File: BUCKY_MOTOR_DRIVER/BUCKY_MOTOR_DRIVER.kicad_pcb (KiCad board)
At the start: 2 copper layers, 26 x 22.6 mm, 8 parts, among them J1 P_INPUTS, J2 INPUTS, J3 OUT, U1 IFX9201SG

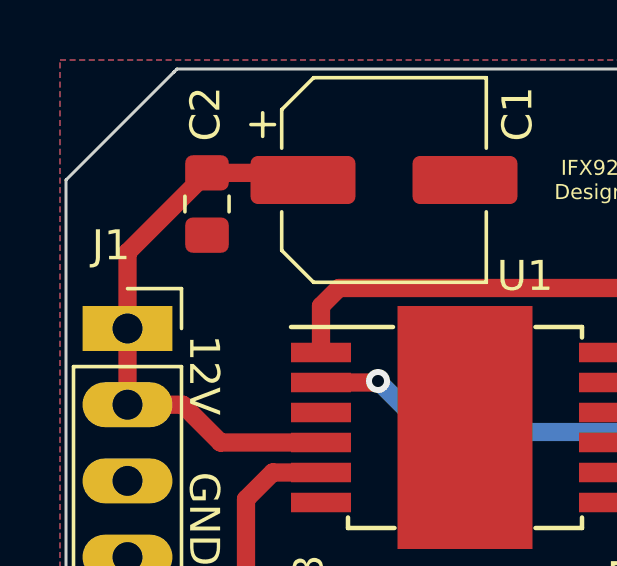
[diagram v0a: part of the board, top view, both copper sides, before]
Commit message: Finished up IR sch, Main, Started Power
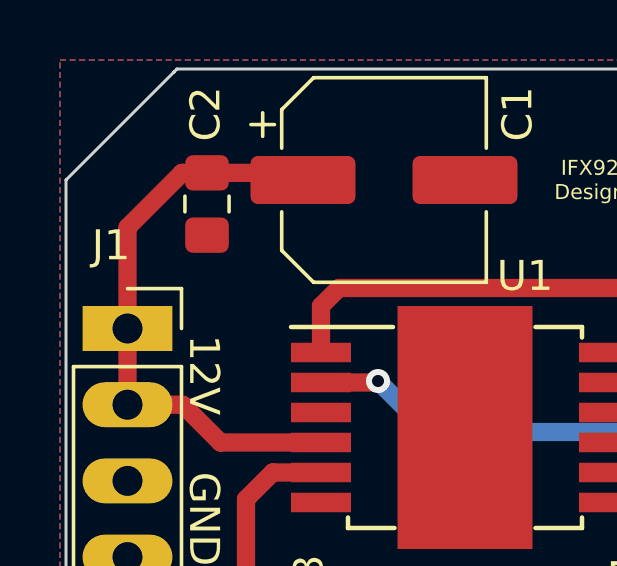
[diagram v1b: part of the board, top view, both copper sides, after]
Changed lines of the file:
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@@
   (segment (start 132.3 59.4) (end 139.4 59.4) (width 0.61) (layer "B.Cu") (net 1))
   (segment (start 122.25 58.49) (end 124.09 58.49) (width 0.61) (layer "F.Cu") (net 3))
-  (segment (start 122.25 55.95) (end 122.25 53.4125) (width 0.61) (layer "F.Cu") (net 3))
   (segment (start 124.09 58.49) (end 125.35 59.75) (width 0.61) (layer "F.Cu") (net 3))
   (segment (start 127.8625 50.7625) (end 128.1 51) (width 0.61) (layer "F.Cu") (net 3))
   (segment (start 124.9 50.7625) (end 127.8625 50.7625) (width 0.61) (layer "F.Cu") (net 3))
+  (segment (start 122.25 55.95) (end 122.25 52.58125) (width 0.61) (layer "F.Cu") (net 3))
+  (segment (start 124.06875 50.7625) (end 124.9 50.7625) (width 0.61) (layer "F.Cu") (net 3))
   (segment (start 125.35 59.75) (end 128.7 59.75) (width 0.61) (layer "F.Cu") (net 3))
   (segment (start 122.25 58.49) (end 122.25 55.95) (width 0.61) (layer "F.Cu") (net 3))
-  (segment (start 122.25 53.4125) (end 124.9 50.7625) (width 0.61) (layer "F.Cu") (net 3))
+  (segment (start 122.25 52.58125) (end 124.06875 50.7625) (width 0.61) (layer "F.Cu") (net 3))
   (segment (start 128.7 60.75) (end 127.09 60.75) (width 0.61) (layer "F.Cu") (net 4))
   (segment (start 126.9 68) (end 132.235 68) (width 0.61) (layer "F.Cu") (net 4))

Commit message: Started POWER
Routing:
- net Net-(C3-Pad1): track 14.9 -> 29.6 mm, vias 0 -> 2
- net Net-(C4-Pad1): track 13.9 -> 26.8 mm, vias 0 -> 2
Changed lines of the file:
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@@
     (fp_line (start -1.27 3.81) (end -1.27 -0.635) (layer "F.Fab") (width 0.1))
     (fp_line (start 1.27 3.81) (end -1.27 3.81) (layer "F.Fab") (width 0.1))
-    (pad "1" thru_hole rect (at 0 0 270) (size 1.7 1.7) (drill 1) (layers *.Cu *.Mask)
+    (pad "1" thru_hole rect (at 0 0 270) (size 3 1.5) (drill 1) (layers *.Cu *.Mask)
       (net 6 "Net-(C4-Pad1)") (pinfunction "Pin_1") (pintype "passive"))
-    (pad "2" thru_hole oval (at 0 2.54 270) (size 1.7 1.7) (drill 1) (layers *.Cu *.Mask)
+    (pad "2" thru_hole oval (at 0 2.54 270) (size 3 1.5) (drill 1) (layers *.Cu *.Mask)
       (net 4 "Net-(C3-Pad1)") (pinfunction "Pin_2") (pintype "passive"))
     (model "${KICAD6_3DMODEL_DIR}/Connector_PinHeader_2.54mm.3dshapes/PinHeader_1x02_P2.54mm_Vertical.wrl"
@@
   (segment (start 122.25 58.49) (end 122.25 55.95) (width 0.61) (layer "F.Cu") (net 3))
   (segment (start 122.25 52.58125) (end 124.06875 50.7625) (width 0.61) (layer "F.Cu") (net 3))
-  (segment (start 128.7 60.75) (end 127.09 60.75) (width 0.61) (layer "F.Cu") (net 4))
-  (segment (start 126.9 68) (end 132.235 68) (width 0.61) (layer "F.Cu") (net 4))
-  (segment (start 127.09 60.75) (end 126.2 61.64) (width 0.61) (layer "F.Cu") (net 4))
-  (segment (start 126.2 67.3) (end 126.9 68) (width 0.61) (layer "F.Cu") (net 4))
-  (segment (start 126.2 61.64) (end 126.2 67.3) (width 0.61) (layer "F.Cu") (net 4))
-  (via (at 123.6 68.9) (size 0.4) (drill 0.2) (layers "F.Cu" "B.Cu") (free) (net 5))
-  (via (at 121.5 66.9) (size 0.4) (drill 0.2) (layers "F.Cu" "B.Cu") (free) (net 5))
-  (via (at 122.6 68) (size 0.4) (drill 0.2) (layers "F.Cu" "B.Cu") (free) (net 5))
-  (segment (start 140.05 61.75) (end 140.7 62.4) (width 0.61) (layer "F.Cu") (net 6))
-  (segment (start 140.2 68) (end 134.775 68) (width 0.61) (layer "F.Cu") (net 6))
-  (segment (start 140.7 62.4) (end 140.7 67.5) (width 0.61) (layer "F.Cu") (net 6))
-  (segment (start 138.3 61.75) (end 140.05 61.75) (width 0.61) (layer "F.Cu") (net 6))
-  (segment (start 140.7 67.5) (end 140.2 68) (width 0.61) (layer "F.Cu") (net 6))
+  (segment (start 128.3 67.8625) (end 132.0975 67.8625) (width 0.61) (layer "F.Cu") (net 4))
+  (segment (start 126.2 61.6) (end 126.2 67.3) (width 0.61) (layer "F.Cu") (net 4))
+  (segment (start 126.7625 67.8625) (end 128.3 67.8625) (width 0.61) (layer "F.Cu") (net 4))
+  (segment (start 128.7 60.75) (end 127.05 60.75) (width 0.61) (layer "F.Cu") (net 4))
+  (segment (start 127.05 60.75) (end 126.2 61.6) (width 0.61) (layer "F.Cu") (net 4))
+  (segment (start 126.2 67.3) (end 126.7625 67.8625) (width 0.61) (layer "F.Cu") (net 4))
+  (segment (start 132.0975 67.8625) (end 132.235 68) (width 0.61) (layer "F.Cu") (net 4))
+  (via (at 128.7 60.75) (size 0.8) (drill 0.4) (layers "F.Cu" "B.Cu") (net 4))
+  (via (at 128.3 67.8625) (size 0.8) (drill 0.4) (layers "F.Cu" "B.Cu") (net 4))
+  (segment (start 128.7 60.75) (end 127.05 60.75) (width 0.61) (layer "B.Cu") (net 4))
+  (segment (start 126.7625 67.8625) (end 128.3 67.8625) (width 0.61) (layer "B.Cu") (net 4))
+  (segment (start 127.05 60.75) (end 126.2 61.6) (width 0.61) (layer "B.Cu") (net 4))
+  (segment (start 126.2 61.6) (end 126.2 67.3) (width 0.61) (layer "B.Cu") (net 4))
+  (segment (start 128.3 67.8625) (end 132.0975 67.8625) (width 0.61) (layer "B.Cu") (net 4))
+  (segment (start 126.2 67.3) (end 126.7625 67.8625) (width 0.61) (layer "B.Cu") (net 4))
+  (via (at 133.6 64.3) (size 0.8) (drill 0.4) (layers "F.Cu" "B.Cu") (free) (net 5))
+  (via (at 128.3 64.3) (size 0.8) (drill 0.4) (layers "F.Cu" "B.Cu") (free) (net 5))
+  (via (at 138.9 64.3) (size 0.8) (drill 0.4) (layers "F.Cu" "B.Cu") (free) (net 5))
+  (segment (start 134.8125 67.9625) (end 134.775 68) (width 0.61) (layer "F.Cu") (net 6))
+  (segment (start 139.75 61.75) (end 140.6 62.6) (width 0.61) (layer "F.Cu") (net 6))
+  (segment (start 140.6 62.6) (end 140.6 67.3) (width 0.61) (layer "F.Cu") (net 6))
+  (segment (start 138.3 61.75) (end 139.75 61.75) (width 0.61) (layer "F.Cu") (net 6))
+  (segment (start 140.6 67.3) (end 139.9375 67.9625) (width 0.61) (layer "F.Cu") (net 6))
+  (segment (start 138.9 67.9625) (end 134.8125 67.9625) (width 0.61) (layer "F.Cu") (net 6))
+  (segment (start 138.9375 67.9625) (end 138.9 67.9625) (width 0.61) (layer "F.Cu") (net 6))
+  (segment (start 139.9375 67.9625) (end 138.9375 67.9625) (width 0.61) (layer "F.Cu") (net 6))
+  (via (at 138.9375 67.9625) (size 0.8) (drill 0.4) (layers "F.Cu" "B.Cu") (net 6))
+  (via (at 138.3 61.75) (size 0.8) (drill 0.4) (layers "F.Cu" "B.Cu") (net 6))
+  (segment (start 140.6 67.3) (end 139.9375 67.9625) (width 0.61) (layer "B.Cu") (net 6))
+  (segment (start 139.9375 67.9625) (end 138.9375 67.9625) (width 0.61) (layer "B.Cu") (net 6))
+  (segment (start 138.9 67.9625) (end 134.8125 67.9625) (width 0.61) (layer "B.Cu") (net 6))
+  (segment (start 140.6 62.6) (end 140.6 67.3) (width 0.61) (layer "B.Cu") (net 6))
+  (segment (start 138.3 61.75) (end 139.75 61.75) (width 0.61) (layer "B.Cu") (net 6))
+  (segment (start 139.75 61.75) (end 140.6 62.6) (width 0.61) (layer "B.Cu") (net 6))
   (segment (start 142.925 54.6) (end 129.3 54.6) (width 0.61) (layer "F.Cu") (net 7))
   (segment (start 128.7 55.2) (end 128.7 56.75) (width 0.61) (layer "F.Cu") (net 7))

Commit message: Finished PCBS
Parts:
- J1, J2: moved to B.Cu
- turned J1 to 180 degrees
- turned J2 to 180 degrees
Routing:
- net GND: vias 3 -> 15
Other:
- board size 26 x 22.6 mm -> 26 x 23.6 mm

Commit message: chore: start on schematics
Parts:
- C3, C4: value 33n -> 10n
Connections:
- net +3V3 renamed +5V
- net Net-(C3-Pad1) renamed /OUT_1
- net Net-(C4-Pad1) renamed /OUT_2
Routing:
- net /OUT_1: track 29.6 -> 14.9 mm, vias 2 -> 0
- net /OUT_2: track 26.8 -> 13.5 mm, vias 2 -> 0
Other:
- board text added: "IFX9201SG Breakout Designed by koen1711"
- board text removed: "IFX9201SG Breakout Designed by Pixeljoch"
